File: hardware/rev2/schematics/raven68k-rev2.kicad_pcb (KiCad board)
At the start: 2 copper layers, 149.9 x 133.3 mm, 78 parts, among them IC1 L5970D013TR, IC2 L5970D013TR, J1 CPLD_JTAG, J2 DUART_IO, J3 RAPC722BK, SW1 RESET_SW, U1 MCP100-465D, U10 28C256, U11 28C256, U12 MT16D832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

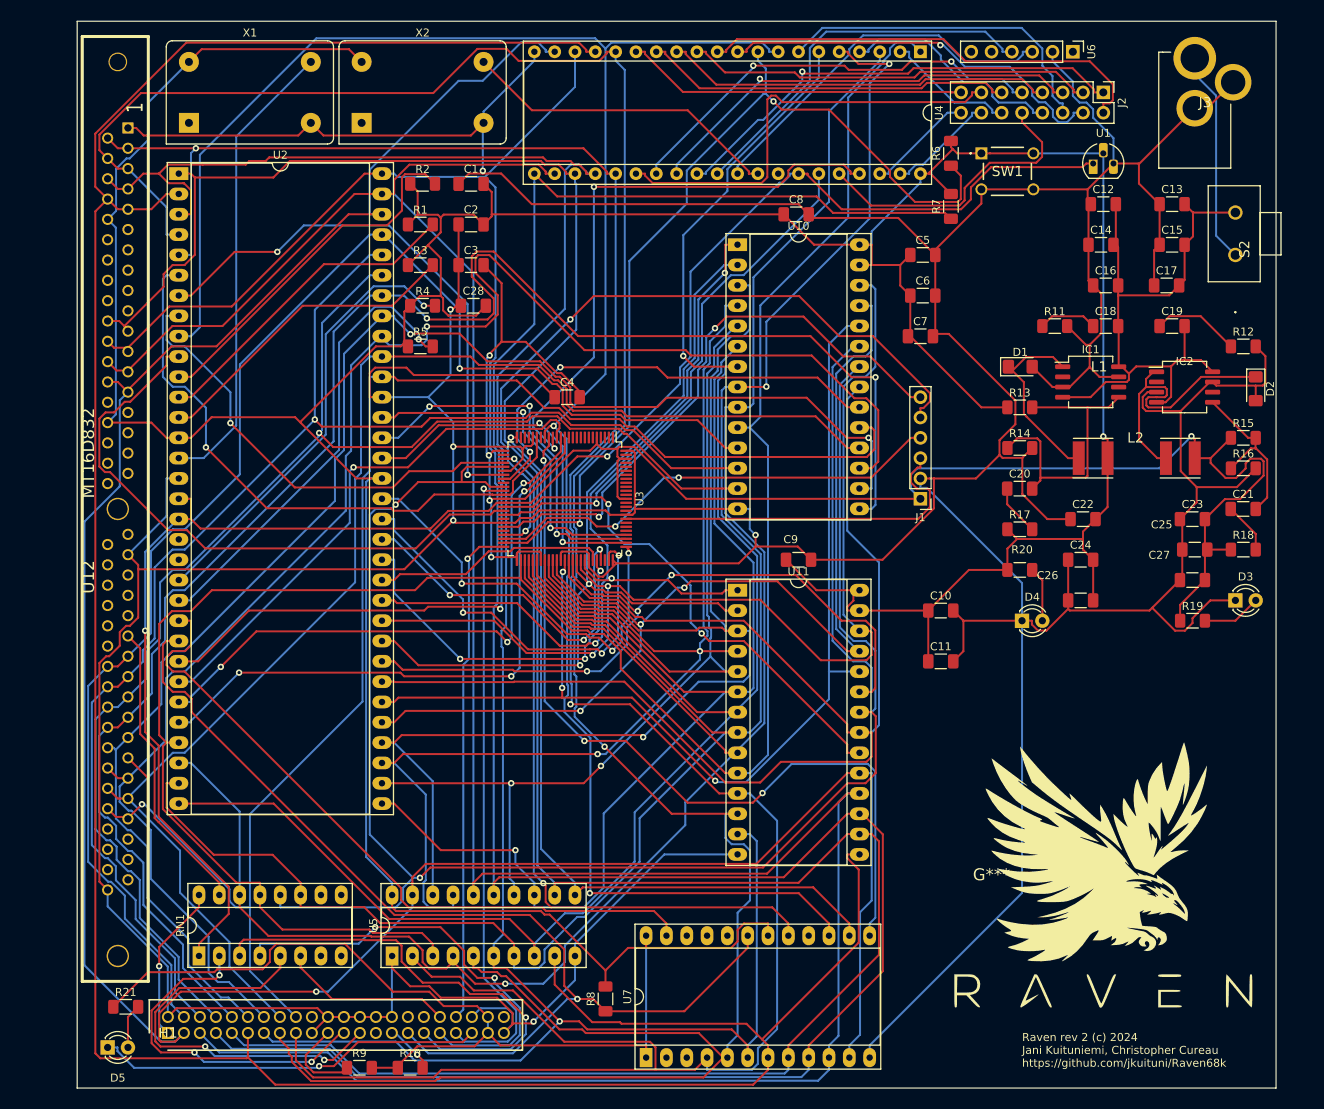
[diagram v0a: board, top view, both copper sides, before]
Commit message: Minor adjustment to add the CLK signal to the CPLD that was forgotten. Re-did the PCB to reflect this change and also edited the component placement a bit.
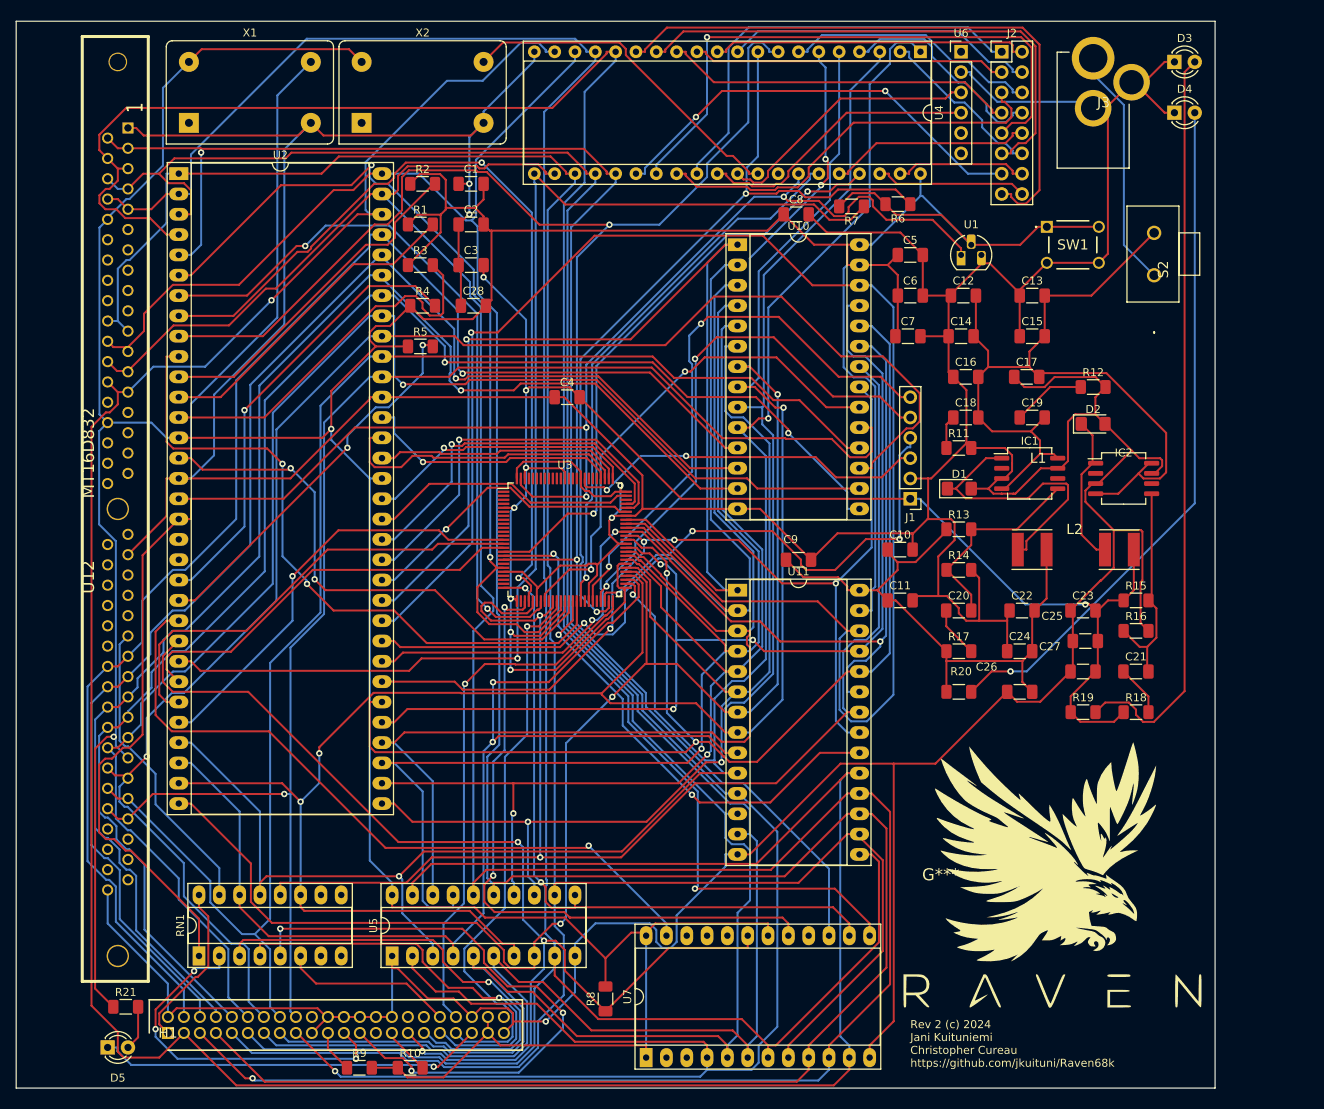
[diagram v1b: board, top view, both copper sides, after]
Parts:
- moved D3 67.7 mm to (147.3, 19.1)
- moved D4 66.3 mm to (147.3, 25.4)
- moved R16 24.3 mm to (142.5, 90.2)
- moved C21 24.3 mm to (142.5, 95.2)
- moved R15 24.3 mm to (142.5, 86.4)
- moved R18 24.3 mm to (142.5, 100.3)
- moved C15 20.9 mm to (129.5, 53.3)
- moved C12 20.9 mm to (120.9, 48.3)
- moved C13 20.9 mm to (129.5, 48.3)
- moved C17 20.9 mm to (128.9, 58.4)
- moved C19 20.9 mm to (129.5, 63.5)
- moved C16 20.9 mm to (121.2, 58.4)
- moved C18 20.9 mm to (121.2, 63.5)
- moved C14 20.9 mm to (120.7, 53.3)
- moved D2 20.8 mm to (137.2, 64.3), turned to 0 degrees
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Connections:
- U3 pad 39: ~{RESET} -> Net-(U2-CLK)
- U3 pad 99: unconnected-(U3-I/O/GSR-Pad99) -> ~{RESET}
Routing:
- net GND: track 944.1 -> 841.1 mm, vias 6 -> 5
- net Net-(D3-A): track 7.40 -> 93.8 mm
- net Net-(D4-A): track 6.88 -> 86.5 mm, vias 0 -> 1
- net A14: track 132.7 -> 206.8 mm, vias 2 -> 1
- net Net-(U2-CLK): track 58.2 -> 124.8 mm, vias 0 -> 2
- net D7: track 319.6 -> 367.2 mm
- net ~{LDS}: track 57.8 -> 105.4 mm, vias 1 -> 2
- net A11: track 166.9 -> 121.4 mm, vias 0 -> 4
- net D3: track 350.6 -> 307.4 mm
- net OP7: track 42.9 -> 77.1 mm
- net ~{OE}: track 215.0 -> 181.5 mm
- net ~{AS}: track 77.1 -> 108.8 mm, vias 1 -> 2
- net A15: track 111.3 -> 142.6 mm, vias 3 -> 1
- net R~{W}: track 250.4 -> 219.6 mm
- net Net-(IC1-COMP): track 79.0 -> 108.9 mm
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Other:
- board text added: "Rev 2 (c) 2024 Jani Kuituniemi Christopher Cureau https://github.com/jkuituni/Raven68k"
- board text removed: "Raven rev 2 (c) 2024 Jani Kuituniemi, Christopher Cureau https://github.com/jkuituni/Raven68k"

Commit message: DRC fixes.
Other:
- board size 149.9 x 133.3 mm -> 146 x 134.6 mm

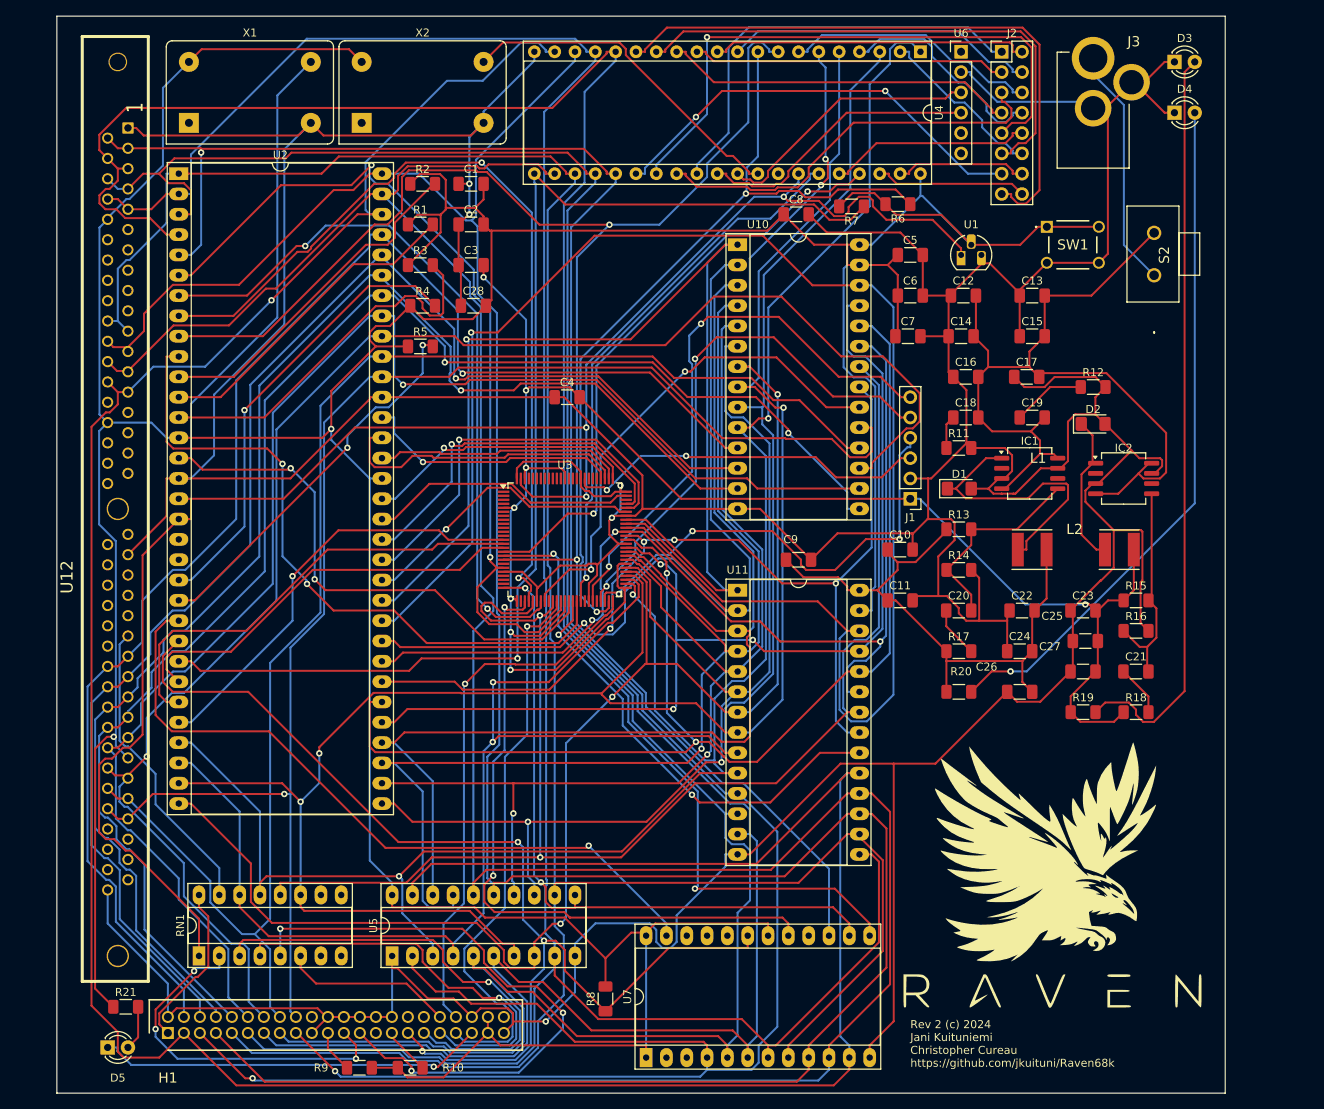
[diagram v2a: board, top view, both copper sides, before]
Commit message: ERC fixes part 2. No more errors reported. Re-routed the PCB.
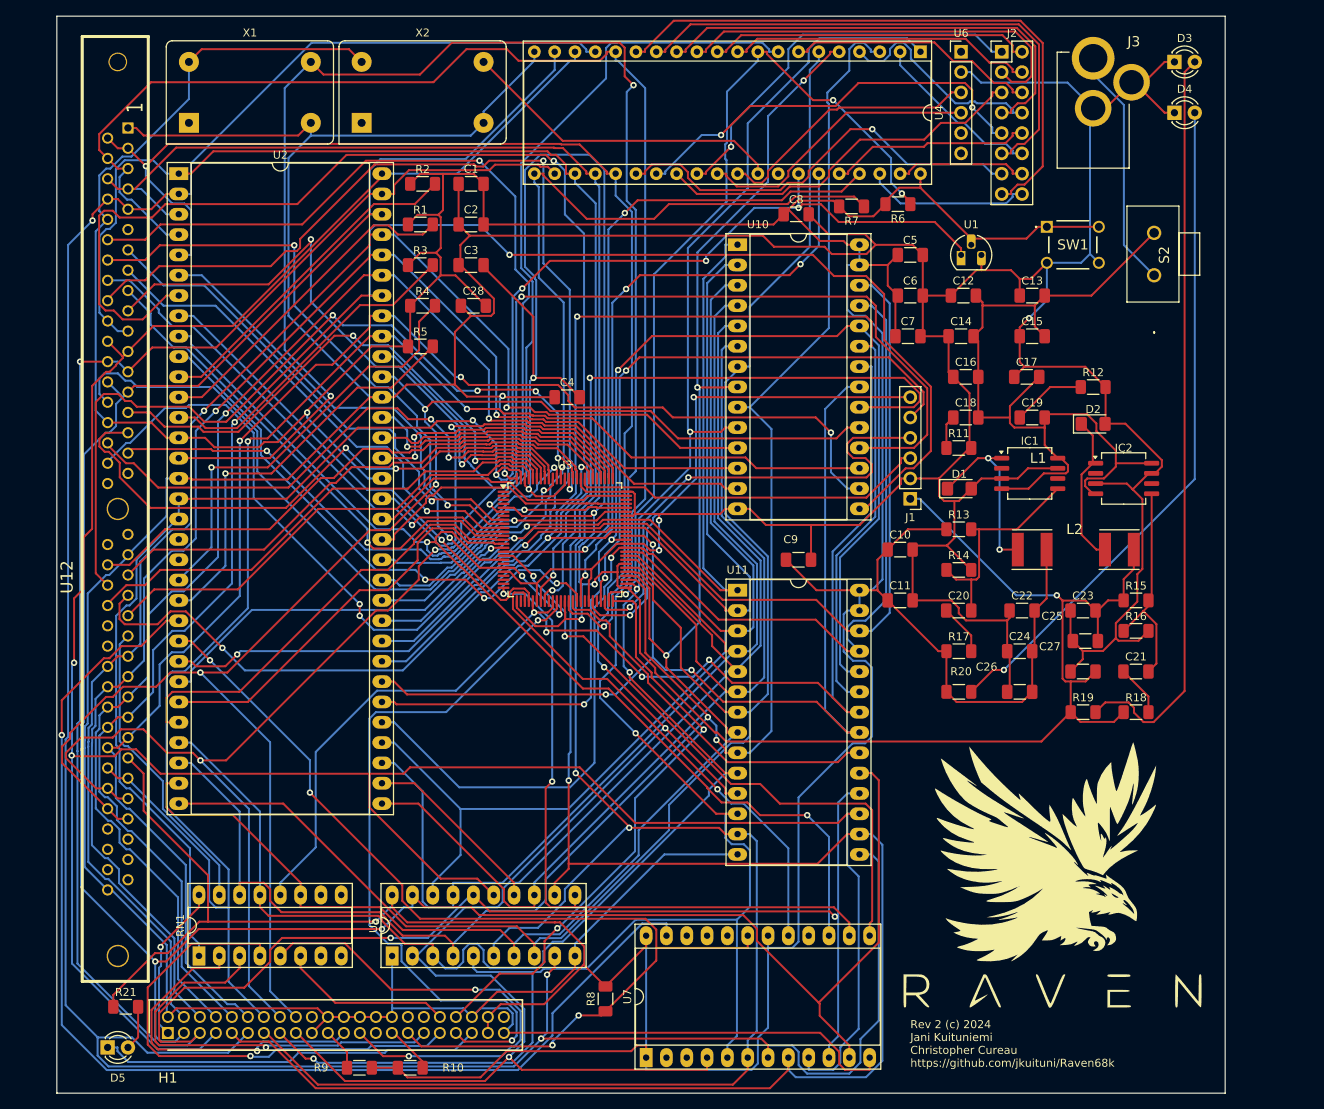
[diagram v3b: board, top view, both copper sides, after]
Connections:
- U12 pad 12: /RAM and ROM/MA0 -> MA0
- U12 pad 13: /RAM and ROM/MA1 -> MA1
- U12 pad 14: /RAM and ROM/MA2 -> MA2
- U12 pad 15: /RAM and ROM/MA3 -> MA3
- U12 pad 16: /RAM and ROM/MA4 -> MA4
- U12 pad 17: /RAM and ROM/MA5 -> MA5
- U12 pad 18: /RAM and ROM/MA6 -> MA6
- U12 pad 19: /RAM and ROM/MA10 -> MA10
- U12 pad 28: /RAM and ROM/MA7 -> MA7
- U12 pad 29: /RAM and ROM/MA11 -> MA11
- U12 pad 31: /RAM and ROM/MA8 -> MA8
- U12 pad 32: /RAM and ROM/MA9 -> MA9
- U12 pad 33: /RAM and ROM/RAS3 -> RAS3
- U12 pad 34: /RAM and ROM/RAS2 -> RAS2
- U12 pad 40: /RAM and ROM/CAS0 -> CAS0
- U12 pad 41: /RAM and ROM/CAS2 -> CAS2
- U12 pad 42: /RAM and ROM/CAS3 -> CAS3
- U12 pad 43: /RAM and ROM/CAS1 -> CAS1
- U12 pad 44: /RAM and ROM/RAS0 -> RAS0
- U12 pad 45: /RAM and ROM/RAS1 -> RAS1
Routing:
- net MA6: track 0.00 -> 106.7 mm, vias 0 -> 2
- net CAS3: track 0.00 -> 103.0 mm, vias 0 -> 4
- net +3V3: track 212.6 -> 315.0 mm, vias 8 -> 6
- net MA0: track 0.00 -> 100.4 mm, vias 0 -> 2
- net RAS2: track 0.00 -> 89.5 mm, vias 0 -> 3
- net A14: track 206.8 -> 118.4 mm
- net MA7: track 0.00 -> 81.5 mm, vias 0 -> 1
- net CAS1: track 0.00 -> 81.0 mm, vias 0 -> 2
- net MA10: track 0.00 -> 77.0 mm, vias 0 -> 2
- net MA2: track 0.00 -> 73.4 mm, vias 0 -> 2
- net MA8: track 0.00 -> 73.3 mm, vias 0 -> 2
- net CAS0: track 0.00 -> 70.3 mm
- net MA9: track 0.00 -> 68.1 mm, vias 0 -> 2
- net MA11: track 0.00 -> 67.7 mm, vias 0 -> 2
- net Net-(U2-CLK): track 124.8 -> 191.2 mm, vias 2 -> 3
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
